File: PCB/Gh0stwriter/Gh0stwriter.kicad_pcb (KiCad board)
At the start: 2 copper layers, 1 part

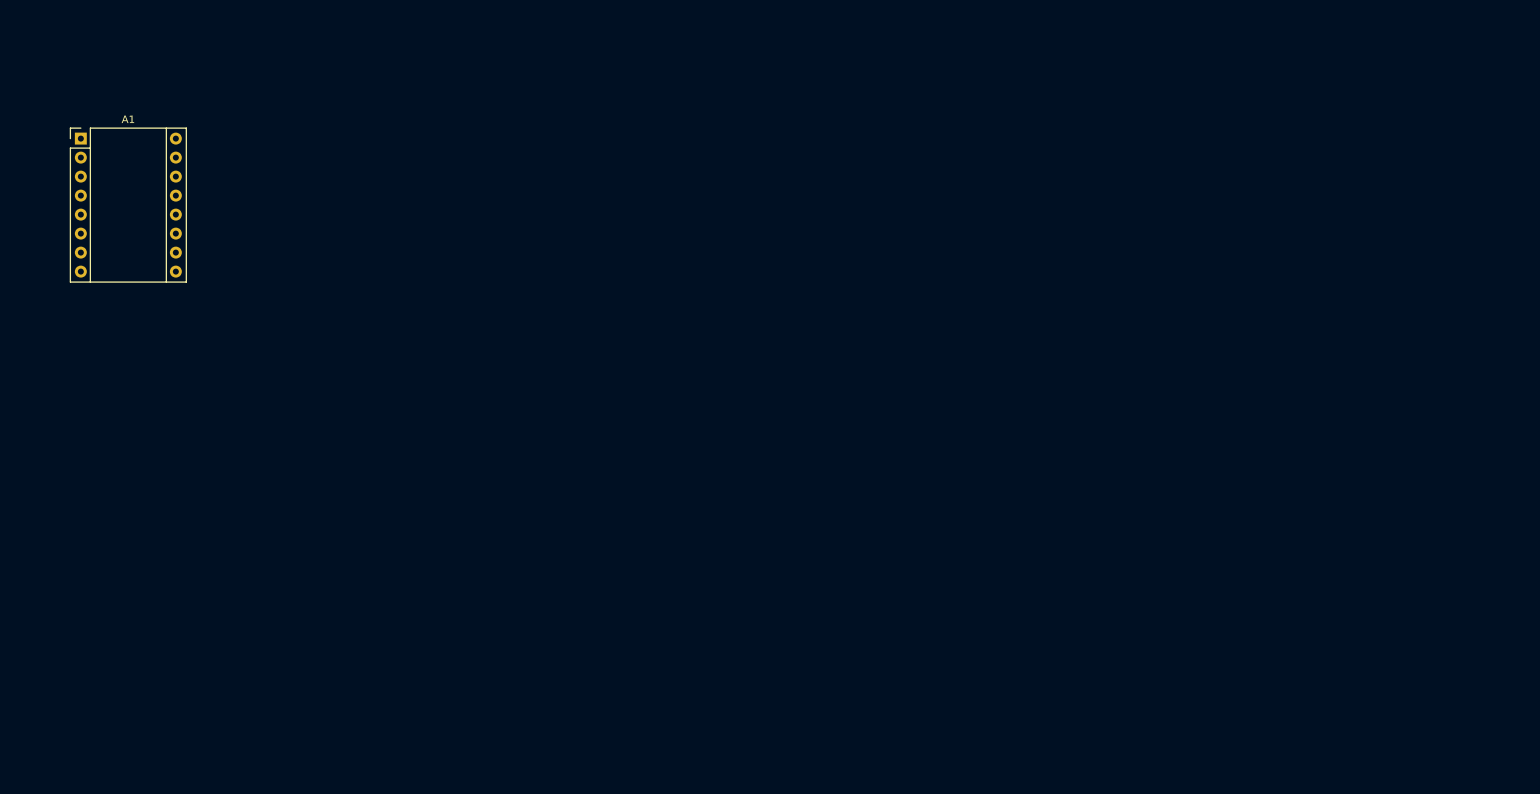
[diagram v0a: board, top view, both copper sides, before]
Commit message: Created pcb outline
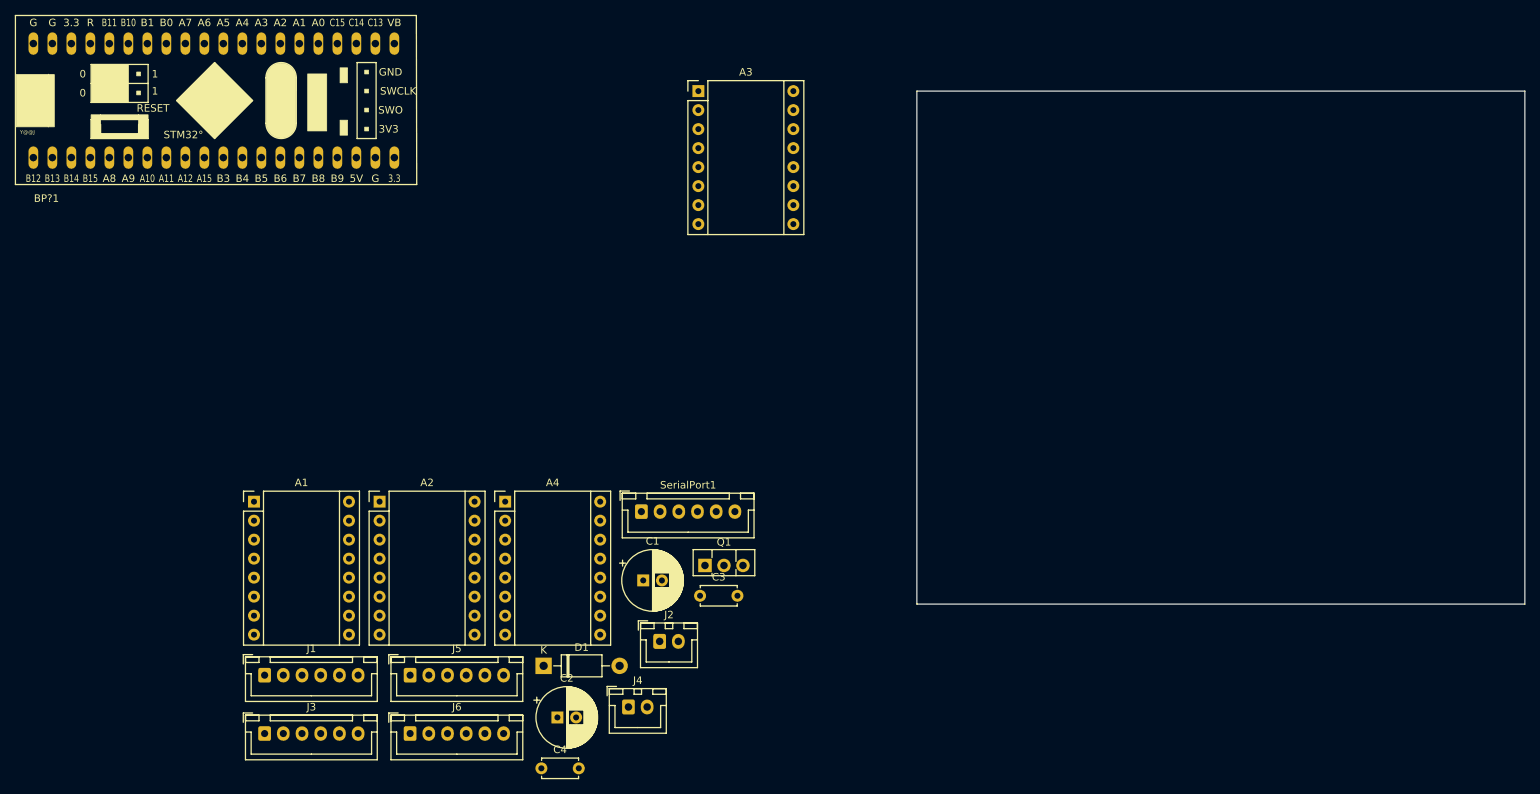
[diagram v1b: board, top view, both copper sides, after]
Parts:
- added A1: Pololu_Breakout_A4988, Module:Pololu_Breakout-16_15.2x20.3mm, F.Cu at (46.0, 79.0)
- added A2: Pololu_Breakout_A4988, Module:Pololu_Breakout-16_15.2x20.3mm, F.Cu at (62.8, 79.0)
- added A4: Pololu_Breakout_A4988, Module:Pololu_Breakout-16_15.2x20.3mm, F.Cu at (79.6, 79.0)
- added BP?1: BluePill_1, bluepill:YAAJ_BluePill, F.Cu at (16.5, 33.0)
- added C1: CP, Capacitor_THT:CP_Radial_D8.0mm_P2.50mm, F.Cu at (98.0, 89.5)
- added C2: CP, Capacitor_THT:CP_Radial_D8.0mm_P2.50mm, F.Cu at (86.6, 107.9)
- added C3: C, Capacitor_THT:C_Disc_D4.7mm_W2.5mm_P5.00mm, F.Cu at (105.6, 91.6)
- added C4: C, Capacitor_THT:C_Disc_D4.7mm_W2.5mm_P5.00mm, F.Cu at (84.4, 114.7)
- added D1: 1N4007, Diode_THT:D_DO-41_SOD81_P10.16mm_Horizontal, F.Cu at (84.7, 101.0)
- added J1: Conn_01x04, Connector_JST:JST_XH_B6B-XH-A_1x06_P2.50mm_Vertical, F.Cu at (47.4, 102.2)
- added J2: Conn_01x02, Connector_JST:JST_XH_B2B-XH-A_1x02_P2.50mm_Vertical, F.Cu at (100.2, 97.7)
- added J3: Conn_01x04, Connector_JST:JST_XH_B6B-XH-A_1x06_P2.50mm_Vertical, F.Cu at (47.4, 110.0)
- added J4: Conn_01x02, Connector_JST:JST_XH_B2B-XH-A_1x02_P2.50mm_Vertical, F.Cu at (96.1, 106.5)
- added J5: Conn_01x04, Connector_JST:JST_XH_B6B-XH-A_1x06_P2.50mm_Vertical, F.Cu at (66.9, 102.2)
- added J6: Conn_01x04, Connector_JST:JST_XH_B6B-XH-A_1x06_P2.50mm_Vertical, F.Cu at (66.9, 110.0)
- added Q1: Q_NPN_Darlington_ECB, Package_TO_SOT_THT:TO-126-3_Vertical, F.Cu at (106.3, 87.5)
- added SerialPort1: Conn_01x06, Connector_JST:JST_XH_B6B-XH-A_1x06_P2.50mm_Vertical, F.Cu at (97.8, 80.3)
- moved A3 82.8 mm to (105.4, 24.1)
- renumbered A1 to A3
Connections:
- A3 pad 1: Net-(A1-Pad1) -> GND
- A3 pad 13: Net-(A1-Pad13) -> ICReset
- A3 pad 2: Net-(A1-Pad2) -> +3V3
- A3 pad 7: Net-(A1-Pad7) -> GND
- A3 pad 8: Net-(A1-Pad8) -> Vdrive
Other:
- board outline added: 81.3 x 68.6 mm

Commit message: Most of pcb finished
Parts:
- added J7: Conn_01x02, TerminalBlock_Phoenix:TerminalBlock_Phoenix_MKDS-1,5-2_1x02_P5.00mm_Horizontal, F.Cu at (203.2, 38.1)
- added R1: R, Resistor_THT:R_Axial_DIN0207_L6.3mm_D2.5mm_P10.16mm_Horizontal, F.Cu at (203.2, 55.9)
- J1, J3, J5, J6: value Conn_01x04 -> Conn_01x06
- SerialPort1: footprint Connector_JST:JST_XH_B6B-XH-A_1x06_P2.50mm_Vertical -> Connector_PinHeader_2.54mm:PinHeader_1x06_P2.54mm_Vertical
- moved BP?1 190.5 mm to (203.2, 71.1), turned to 180 degrees
- moved J6 151.9 mm to (193.0, 25.4), turned to 180 degrees
- moved J3 130.9 mm to (147.2, 25.4), turned to 180 degrees
- moved J5 128.6 mm to (170.1, 25.4), turned to 180 degrees
- moved A4 123.4 mm to (193.0, 30.5), turned to 270 degrees
- moved J4 123.2 mm to (203.2, 45.7), turned to 180 degrees
- moved J1 111.2 mm to (147.3, 53.3), turned to 180 degrees
- moved A1 103.4 mm to (147.3, 58.4), turned to 270 degrees
- moved Q1 98.0 mm to (198.1, 53.3)
- moved A2 97.5 mm to (147.3, 30.5), turned to 270 degrees
- moved SerialPort1 96.7 mm to (193.0, 63.5), turned to 270 degrees
- moved A3 65.1 mm to (170.2, 30.5), turned to 270 degrees
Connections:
- BP?1 pad 1: ICReset -> Hammer
- BP?1 pad 2: Net-(BP?1-Pad2) -> ICReset
- J1 pad 1: Net-(A4-Pad3) -> Net-(J1-Pad1)
- J1 pad 2: Net-(A4-Pad4) -> Net-(J1-Pad2)
- J1 pad 3: Net-(A4-Pad5) -> Net-(A1-Pad3)
- J1 pad 4: Net-(A4-Pad6) -> Net-(A1-Pad4)
- J1 pad 5: (no net) -> Net-(A1-Pad5)
- J1 pad 6: (no net) -> Net-(A1-Pad6)
- J3 pad 1: Net-(A1-Pad3) -> Net-(J3-Pad1)
- J3 pad 2: Net-(A1-Pad4) -> Net-(J3-Pad2)
- J3 pad 3: Net-(A1-Pad5) -> Net-(A2-Pad3)
- J3 pad 4: Net-(A1-Pad6) -> Net-(A2-Pad4)
- J3 pad 5: (no net) -> Net-(A2-Pad5)
- J3 pad 6: (no net) -> Net-(A2-Pad6)
- J5 pad 1: Net-(A2-Pad3) -> Net-(J5-Pad1)
- J5 pad 2: Net-(A2-Pad4) -> Net-(J5-Pad2)
- J5 pad 3: Net-(A2-Pad5) -> Net-(A3-Pad3)
- J5 pad 4: Net-(A2-Pad6) -> Net-(A3-Pad4)
- J5 pad 5: (no net) -> Net-(A3-Pad5)
- J5 pad 6: (no net) -> Net-(A3-Pad6)
- J6 pad 1: Net-(A3-Pad3) -> Net-(J6-Pad1)
- J6 pad 2: Net-(A3-Pad4) -> Net-(J6-Pad2)
- J6 pad 3: Net-(A3-Pad5) -> Net-(A4-Pad3)
- J6 pad 4: Net-(A3-Pad6) -> Net-(A4-Pad4)
- J6 pad 5: (no net) -> Net-(A4-Pad5)
- J6 pad 6: (no net) -> Net-(A4-Pad6)
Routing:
- net +3V3: track 0.00 -> 165.1 mm, vias 0 -> 4
- net GND: track 0.00 -> 155.7 mm, vias 0 -> 3
- net Vdrive: track 0.00 -> 121.9 mm, vias 0 -> 2
- net Net-(A4-Pad6): track 0.00 -> 5.16 mm
- net Net-(A1-Pad6): track 0.00 -> 5.16 mm
- net Net-(A4-Pad5): track 0.00 -> 5.15 mm
- net Net-(A1-Pad5): track 0.00 -> 5.15 mm
- net Net-(A4-Pad4): track 0.00 -> 5.13 mm
- net Net-(A2-Pad6): track 0.00 -> 5.13 mm
- net Net-(A1-Pad4): track 0.00 -> 5.13 mm
- net Net-(A3-Pad6): track 0.00 -> 5.11 mm
- net Net-(A2-Pad5): track 0.00 -> 5.11 mm
- net Net-(A4-Pad3): track 0.00 -> 5.11 mm
- net Net-(A1-Pad3): track 0.00 -> 5.11 mm
- net Net-(A2-Pad4): track 0.00 -> 5.10 mm
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
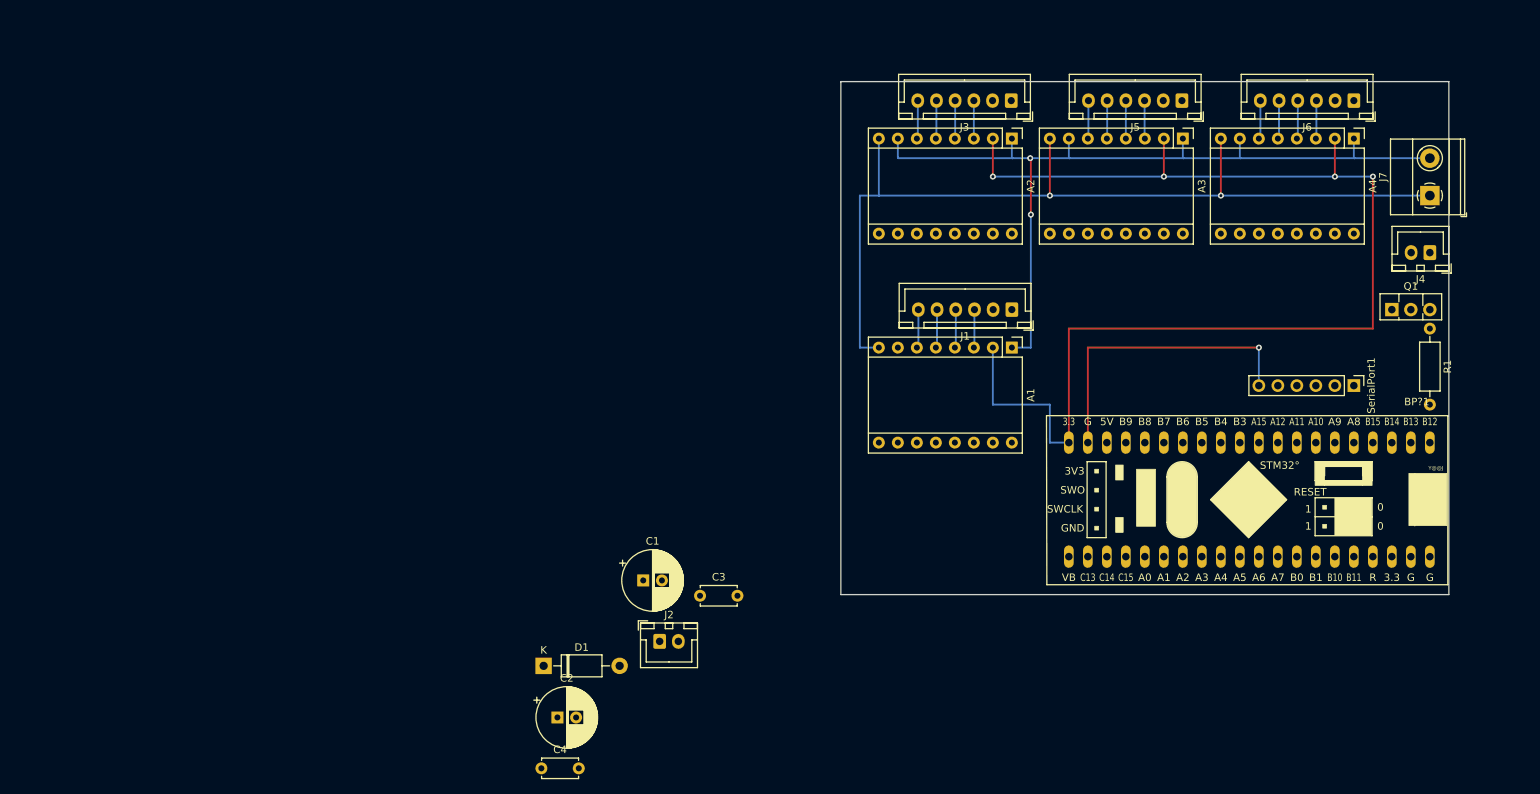
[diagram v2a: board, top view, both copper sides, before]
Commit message: Serial comunication added
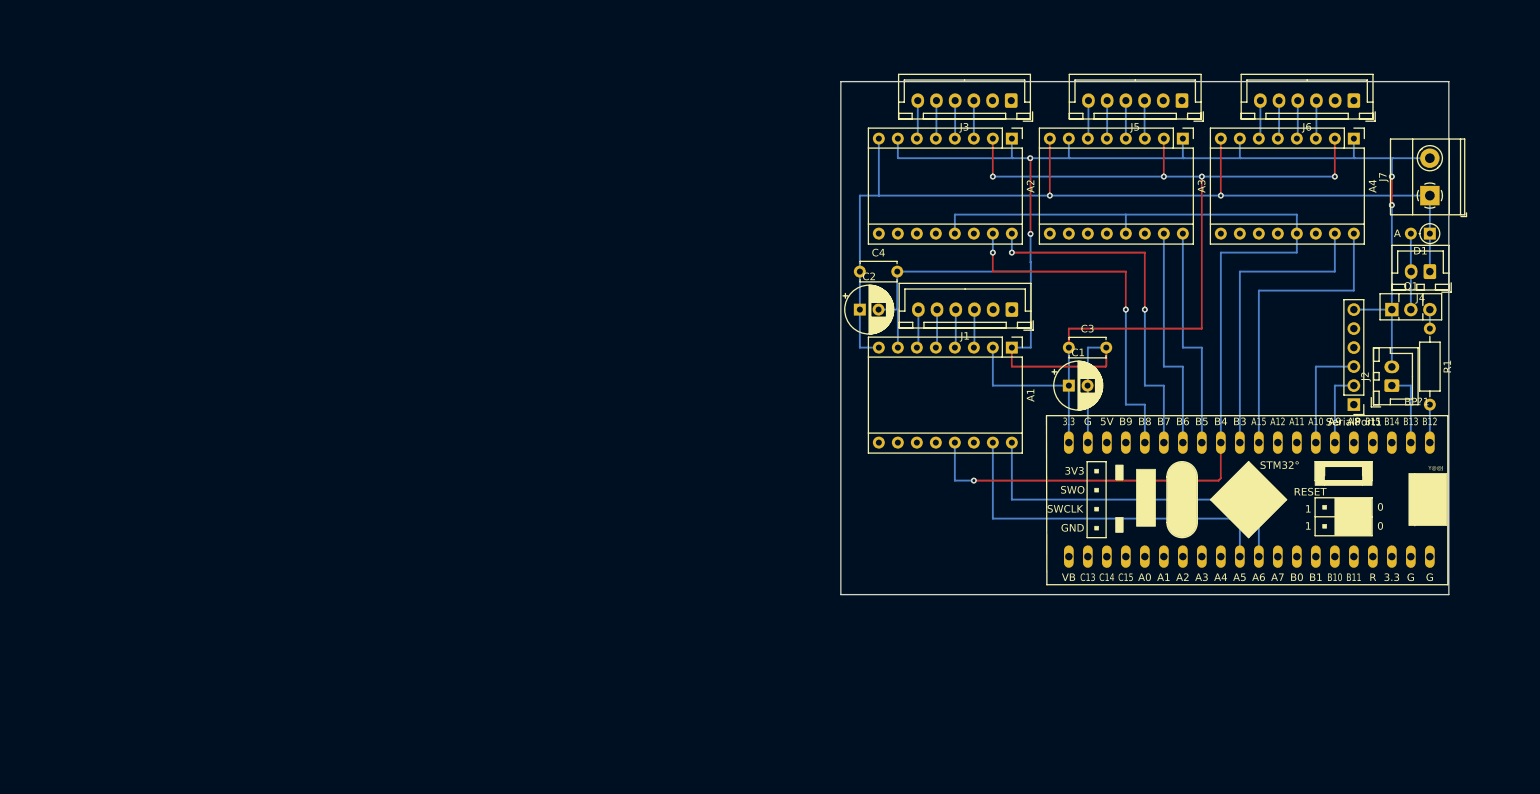
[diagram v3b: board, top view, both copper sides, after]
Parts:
- C1, C2: footprint Capacitor_THT:CP_Radial_D8.0mm_P2.50mm -> Capacitor_THT:CP_Radial_D6.3mm_P2.50mm
- D1: footprint Diode_THT:D_DO-41_SOD81_P10.16mm_Horizontal -> Diode_THT:D_DO-35_SOD27_P2.54mm_Vertical_AnodeUp
- moved D1 131.8 mm to (203.2, 43.2), turned to 180 degrees
- moved J2 103.7 mm to (198.1, 63.5), turned to 90 degrees
- moved C4 78.9 mm to (127.0, 48.3)
- moved C2 67.9 mm to (127.0, 53.3)
- moved C1 62.6 mm to (154.9, 63.5)
- moved C3 59.4 mm to (154.9, 58.4)
- moved SerialPort1 2.54 mm to (193.0, 66.0), turned to 180 degrees
- moved J4 2.54 mm to (203.2, 48.3)
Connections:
- A1 pad 15: Net-(A1-Pad15) -> A1STP
- A1 pad 16: Net-(A1-Pad16) -> A1DIR
- A2 pad 15: Net-(A2-Pad15) -> A2STP
- A2 pad 16: Net-(A2-Pad16) -> A2DIR
- A3 pad 13: ICReset -> Net-(A3-Pad13)
- A3 pad 15: Net-(A3-Pad15) -> A3STP
- A3 pad 16: Net-(A3-Pad16) -> A3DIR
- A4 pad 15: Net-(A4-Pad15) -> A4STP
- A4 pad 16: Net-(A4-Pad16) -> A4DIR
- BP?1 pad 10: Net-(BP?1-Pad10) -> A4DIR
- BP?1 pad 11: Net-(BP?1-Pad11) -> A4STP
- BP?1 pad 12: Net-(BP?1-Pad12) -> ICReset
- BP?1 pad 13: Net-(BP?1-Pad13) -> A3DIR
- BP?1 pad 14: Net-(BP?1-Pad14) -> A3STP
- BP?1 pad 15: Net-(BP?1-Pad15) -> A2DIR
- BP?1 pad 16: Net-(BP?1-Pad16) -> A2STP
- BP?1 pad 2: ICReset -> Endstop
- BP?1 pad 30: Net-(BP?1-Pad30) -> A1STP
- BP?1 pad 31: Net-(BP?1-Pad31) -> A1DIR
- BP?1 pad 39: GND -> Net-(BP?1-Pad39)
- BP?1 pad 40: GND -> Net-(BP?1-Pad40)
- J2 pad 1: Net-(J2-Pad1) -> Endstop
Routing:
- net ICReset: track 0.00 -> 137.0 mm, vias 0 -> 1
- net GND: track 155.7 -> 211.5 mm, vias 3 -> 4
- net A1STP: track 0.00 -> 48.3 mm
- net A1DIR: track 0.00 -> 48.3 mm
- net A2STP: track 0.00 -> 48.3 mm, vias 0 -> 2
- net A2DIR: track 0.00 -> 48.3 mm, vias 0 -> 2
- net A4STP: track 0.00 -> 40.6 mm
- net A4DIR: track 0.00 -> 40.6 mm
- net +3V3: track 165.1 -> 129.5 mm
- net A3DIR: track 0.00 -> 30.5 mm
- net A3STP: track 0.00 -> 30.5 mm
- net PA10: track 0.00 -> 15.2 mm
- net Net-(D1-Pad2): track 0.00 -> 10.2 mm
- net Vdrive: track 121.9 -> 132.1 mm
- net PA9: track 0.00 -> 10.2 mm
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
